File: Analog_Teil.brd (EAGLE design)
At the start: 160 x 100 mm, 0 parts

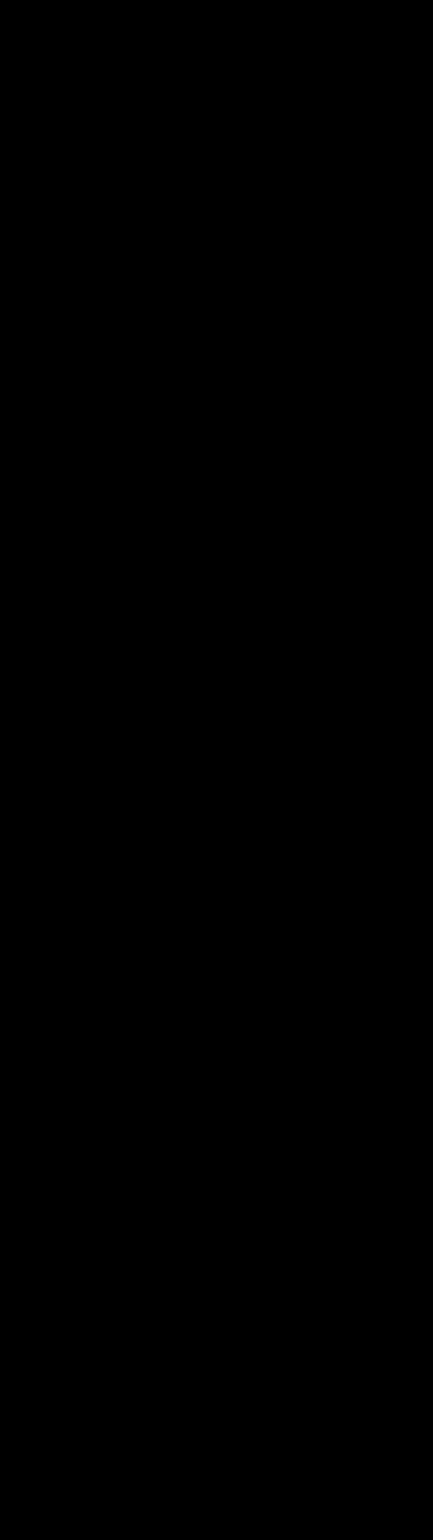
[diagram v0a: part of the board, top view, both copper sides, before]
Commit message: Filterstufe ohne Schutzeinrichtungen und ohne Spannungsversorgung
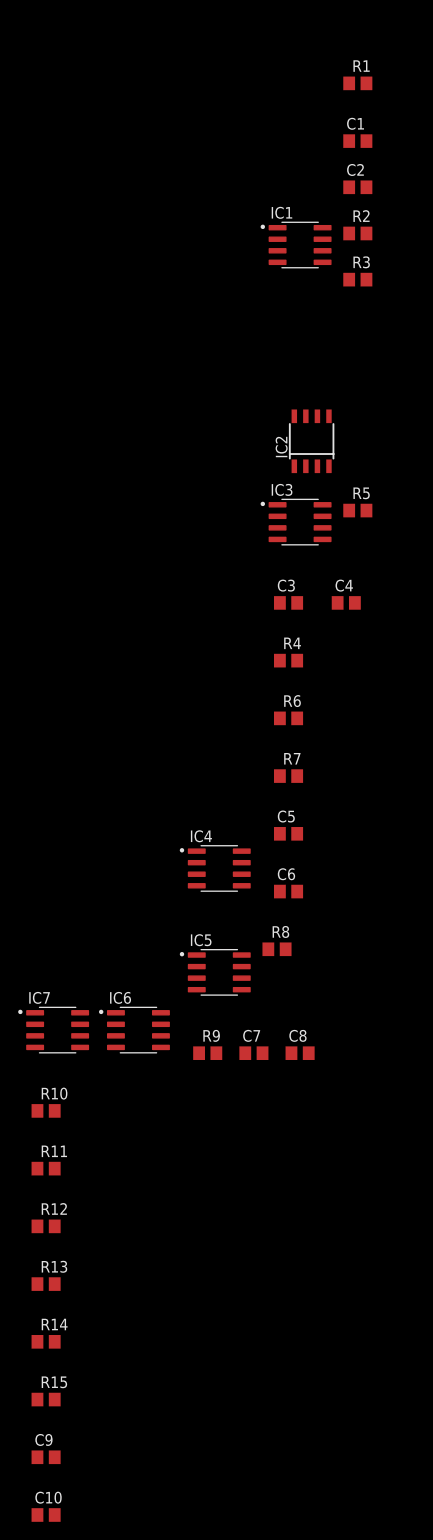
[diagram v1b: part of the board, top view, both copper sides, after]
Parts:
- added C1, C10, C2, C3, C4: 470n, rcl:C0805
- added C5, C7, C9: 4.7n, rcl:C0805
- added C6, C8: 10n, rcl:C0805
- added IC1, IC3, IC4, IC5, IC6, IC7: OPA388, OPA388:SOIC127P600X175-8N
- added IC2: INA828ID, INA828ID:SOIC8
- added R1: 50k, rcl:R0805
- added R10, R11: 138k, rcl:R0805
- added R12, R15: 6.8k, rcl:R0805
- added R13, R14, R3, R5: 100k, rcl:R0805
- added R2, R4: 48k, rcl:R0805
- added R6, R7, R8, R9: 47k, rcl:R0805
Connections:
- new net AGND: C5.1, C7.1, R3.1, R5.1
- new net GND1: IC2.5
- new net N$1: IC2.1, R1.1
- new net N$10: IC3.2, IC3.6, R4.2, R6.1
- new net N$11: C5.2, IC4.3, R7.2
- new net N$12: C8.1, R8.2, R9.1
- new net N$13: C6.2, IC4.2, IC4.6, R8.1
- new net N$14: C7.2, IC5.3, R9.2
- new net N$15: C10.1, C8.2, IC5.2, IC5.6, R11.1, R14.1
- new net N$17: C10.2, IC6.3, R10.2, R11.2, R12.2
- new net N$18: C9.1, IC7.6, R12.1
- new net N$19: C9.2, IC6.2, R15.1
- new net N$2: IC2.8, R1.2
- new net N$20: IC7.2, R15.2
- new net N$21: IC6.6, R13.2
- new net N$22: IC7.3, R13.1, R14.2
- new net N$3: C1.2, C2.1, R2.1
- new net N$4: C2.2, IC1.3, R3.2
- new net N$5: C1.1, IC2.6
- new net N$6: C3.1, IC1.2, IC1.6, R2.2
- new net N$7: C3.2, C4.1, R4.1
- new net N$8: C4.2, IC3.3, R5.2
- new net N$9: C6.1, R6.2, R7.1
- new net V+: IC1.7, IC3.7, IC4.7, IC5.7, IC6.7, IC7.7
- new net V-: IC1.4, IC3.4, IC4.4, IC5.4, IC6.4, IC7.4
